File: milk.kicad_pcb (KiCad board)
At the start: 2 copper layers, 19.2 x 39.4 mm, 18 parts, among them J1 USB_C_Receptacle_USB2.0, J2 RGB, J3 DIP-8_W7.62mm_Socket, SW1 SW_Push, SW2 SW_Push, SW3 SW_Push_Reset, U1 ATtiny85-20SU

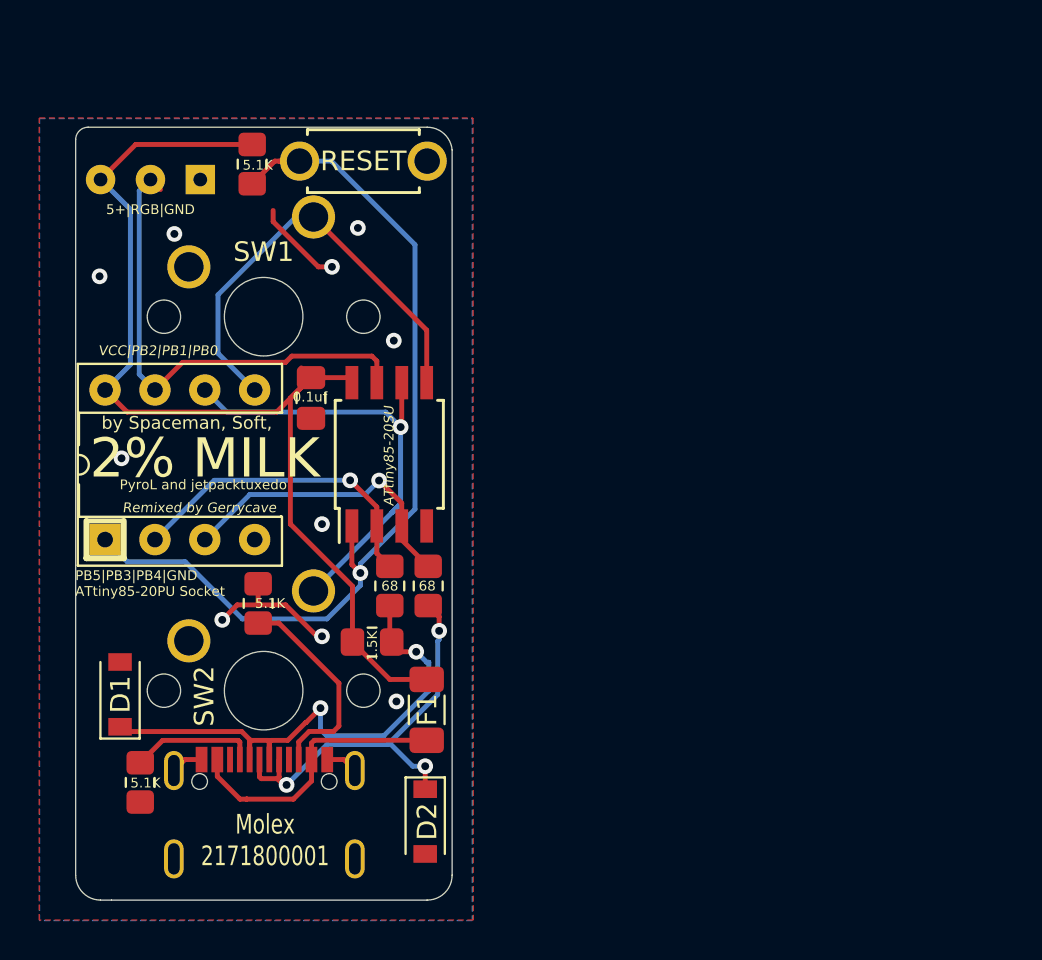
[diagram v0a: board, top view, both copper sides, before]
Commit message: Redo routing, add unsolderable RGB leds
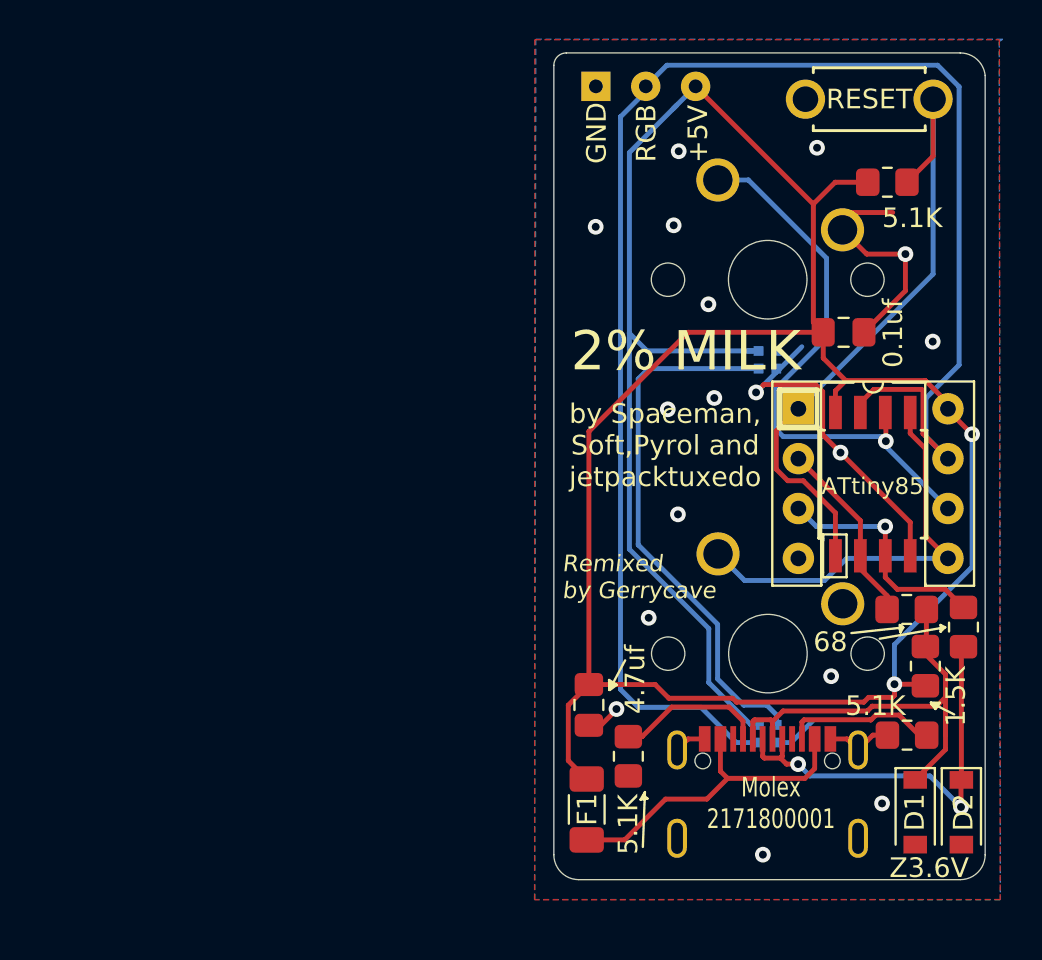
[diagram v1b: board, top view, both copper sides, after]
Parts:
- removed ?: LOGO, silks:40logo
- added C2: 4.7uf, Capacitor_SMD:C_0805_2012Metric_Pad1.18x1.45mm_HandSolder, F.Cu at (197.6, 90.3)
- added D3: SK6805, LED_SMD:LED_SK6812_EC15_1.5x1.5mm, B.Cu at (206.7, 91.7)
- added D4: SK6805, LED_SMD:LED_SK6812_EC15_1.5x1.5mm, B.Cu at (206.7, 72.7)
- added G***: LOGO, footprints:40logo, B.Cu at (201.1, 77.1)
- J3: value DIP-8_W7.62mm_Socket -> DIP-8 Socket
- SW1, SW2: footprint Button_Switch_Keyboard:SW_Cherry_MX_1.00u_PCB -> footprints:SW_Cherry_MX_1.00u_PCB-2mm; moved to B.Cu
- moved D1 40.9 mm to (214.2, 95.7), turned to 270 degrees
- moved J3 35.9 mm to (208.3, 75.2), turned to 0 degrees
- moved R2 33.7 mm to (213.8, 91.8), turned to 0 degrees
- moved R6 32.4 mm to (212.8, 63.6), turned to 180 degrees
- moved SW2 29.4 mm to (204.2, 63.5), turned to 180 degrees
- moved R5 28.2 mm to (214.7, 88.3), turned to 90 degrees
- moved R4 27.3 mm to (216.7, 86.3)
- moved C1 27.3 mm to (210.6, 71.3), turned to 0 degrees
- moved D2 27.3 mm to (216.6, 95.7)
- moved SW1 26.8 mm to (204.2, 82.6), turned to 180 degrees
- moved R3 26.4 mm to (213.8, 85.4), turned to 0 degrees
- moved SW3 26.0 mm to (211.9, 59.4), turned to 0 degrees
- moved J1 25.7 mm to (206.7, 100.0)
- moved R1 24.9 mm to (199.6, 92.9)
- moved U1 24.7 mm to (212.1, 79.0)
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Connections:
- J1 pad : GND -> (no net)
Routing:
- net +5V: track 54.9 -> 140.9 mm, vias 0 -> 2
- net RGB: track 26.3 -> 84.1 mm
- net Net-(D3-Pad1): track 0.00 -> 27.6 mm
- net GND: track 15.2 -> 38.0 mm, vias 10 -> 17
- net RST: track 48.0 -> 33.1 mm, vias 1 -> 0
- net PB3: track 16.4 -> 9.55 mm, vias 1 -> 0
- net D-: track 28.4 -> 23.3 mm, vias 2 -> 0
- net PB1: track 23.9 -> 29.0 mm
- net PB4: track 15.5 -> 12.1 mm
- net Net-(J1-PadB5): track 10.8 -> 7.80 mm
- net VCC: track 14.4 -> 16.8 mm
- net PB0: track 23.0 -> 21.0 mm
- net Net-(J1-PadA5): track 6.47 -> 7.67 mm
- net D+: track 22.0 -> 21.3 mm, vias 3 -> 2
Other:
- board size 19.2 x 39.4 mm -> 22 x 42.1 mm
- board text added: "+5V"
- board text added: "4.7uf"
- board text added: "ATtiny85"
- board text added: "GND"
- board text added: "RGB"
- board text added: "Z3.6V"
- board text added: "by Spaceman, Soft,Pyrol and jetpacktuxedo"
- board text removed: "5+|RGB|GND"
- board text removed: "ATtiny85-20SU"
- board text removed: "PB5|PB3|PB4|GND ATtiny85-20PU Socket"
- board text removed: "PyroL and jetpacktuxedo"
- board text removed: "VCC|PB2|PB1|PB0"
- board text removed: "by Spaceman, Soft,"

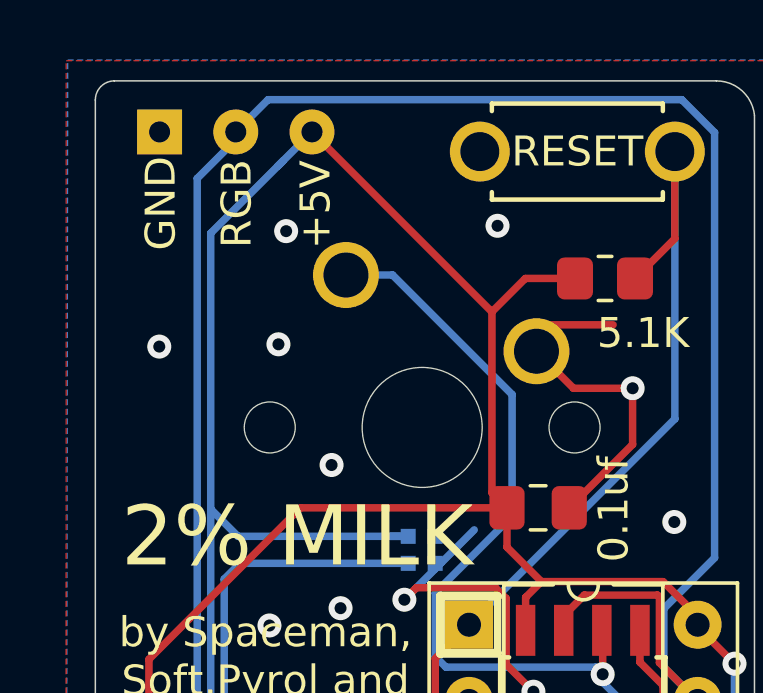
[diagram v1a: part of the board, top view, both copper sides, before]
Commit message: Fix RGB header orientation
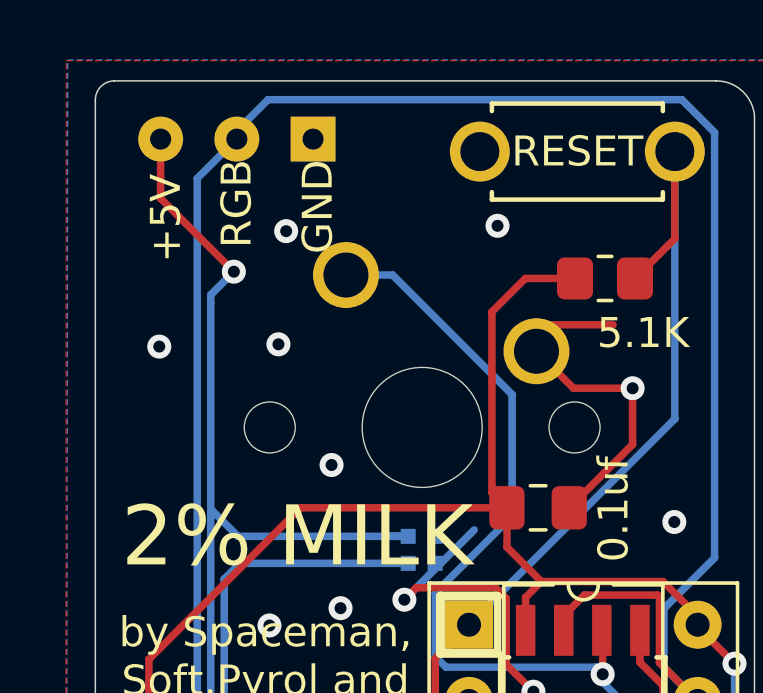
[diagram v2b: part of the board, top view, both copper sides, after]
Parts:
- moved J2 5.12 mm to (203.1, 59.0), turned to 270 degrees
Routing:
- net +5V: track 140.9 -> 131.8 mm, vias 2 -> 3
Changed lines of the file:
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@@
     (thickness 1.6)
     (drawings 64)
-    (tracks 231)
+    (tracks 232)
     (zones 0)
     (modules 21)
@@
       (effects (font (size 1 1) (thickness 0.15)))
     )
-    (fp_text user %R (at 0 0 90) (layer F.Fab)
-      (effects (font (size 0.5 0.5) (thickness 0.08)))
-    )
     (fp_line (start -1 0.625) (end -1 -0.625) (layer F.Fab) (width 0.1))
     (fp_line (start -1 -0.625) (end 1 -0.625) (layer F.Fab) (width 0.1))
@@
     (fp_line (start 1.88 -0.98) (end 1.88 0.98) (layer F.CrtYd) (width 0.05))
     (fp_line (start 1.88 0.98) (end -1.88 0.98) (layer F.CrtYd) (width 0.05))
+    (fp_text user %R (at 0 0 90) (layer F.Fab)
+      (effects (font (size 0.5 0.5) (thickness 0.08)))
+    )
     (pad 2 smd roundrect (at 1.0375 0 90) (size 1.175 1.45) (layers F.Cu F.Paste F.Mask) (roundrect_rratio 0.2127659574468085)
       (net 3 +5V))
@@
     (pad 1 thru_hole rect (at 0 0) (size 1.6 1.6) (drill 0.8) (layers *.Cu *.Mask)
       (net 8 RST))
-    (model ${KISYS3DMOD}/Package_DIP.3dshapes/DIP-8_W7.62mm_Socket.wrl
-      (at (xyz 0 0 0))
-      (scale (xyz 1 1 1))
-      (rotate (xyz 0 0 0))
-    )
   )
   (module footprints:SW_Cherry_MX_1.00u_PCB-2mm (layer B.Cu)
@@
   )
   (module Connector_PinHeader_2.54mm:PinHeader_1x03_P2.54mm_Vertical (layer F.Cu)
-    (at 197.94982 58.7502 90)
+    (at 203.06538 58.98896 270)
     (descr "Through hole straight pin header, 1x03, 2.54mm pitch, single row")
     (tags "Through hole pin header THT 1x03 2.54mm single row")
@@
       (effects (font (size 1 1) (thickness 0.15)))
     )
-    (pad 1 thru_hole rect (at 0 0 90) (size 1.5 1.5) (drill 0.7) (layers *.Cu *.Mask)
-      (net 1 GND))
-    (pad 2 thru_hole circle (at 0 2.54 90) (size 1.5 1.5) (drill 0.7) (layers *.Cu *.Mask)
+    (pad 1 thru_hole rect (at 0 0 270) (size 1.5 1.5) (drill 0.7) (layers *.Cu *.Mask)
+      (net 1 GND))
+    (pad 2 thru_hole circle (at 0 2.54 270) (size 1.5 1.5) (drill 0.7) (layers *.Cu *.Mask)
       (net 9 RGB))
-    (pad 3 thru_hole circle (at 0 5.08 90) (size 1.5 1.5) (drill 0.7) (layers *.Cu *.Mask)
+    (pad 3 thru_hole circle (at 0 5.08 270) (size 1.5 1.5) (drill 0.7) (layers *.Cu *.Mask)
       (net 3 +5V))
   )
@@
     (effects (font (size 1 1) (thickness 0.15)))
   )
-  (gr_text +5V (at 203.1492 61.17082 90) (layer F.SilkS)
+  (gr_text +5V (at 198.16318 61.62548 90) (layer F.SilkS)
     (effects (font (size 1 1) (thickness 0.15)))
   )
@@
     (arrow2b (pts (xy 219.9305 57.05602) (xy 220.516921 58.182524)))
   )
-  (gr_text GND (at 197.98792 61.13018 90) (layer F.SilkS)
+  (gr_text GND (at 203.2254 61.24448 90) (layer F.SilkS)
     (effects (font (size 1 1) (thickness 0.15)))
   )
-  (via (at 216.5477 95.46082) (size 0.8) (drill 0.4) (layers F.Cu B.Cu) (net 5))
-  (via (at 217.11412 76.47432) (size 0.8) (drill 0.4) (layers F.Cu B.Cu) (net 3))
+  (via (at 200.42632 63.40856) (size 0.8) (drill 0.4) (layers F.Cu B.Cu) (net 3))
   (via (at 198.99884 90.46972) (size 0.8) (drill 0.4) (layers F.Cu B.Cu) (net 1))
   (segment (start 202.64504 91.99408) (end 202.08504 92.55408) (width 0.25) (layer F.Cu) (net 1))
@@
   (segment (start 199.41928 97.13588) (end 201.4982 95.05696) (width 0.25) (layer F.Cu) (net 2))
   (segment (start 197.48246 97.13588) (end 199.41928 97.13588) (width 0.25) (layer F.Cu) (net 2))
+  (via (at 217.11412 76.47432) (size 0.8) (drill 0.4) (layers F.Cu B.Cu) (net 3))
   (segment (start 215.88476 74.890688) (end 215.88476 75.17638) (width 0.25) (layer F.Cu) (net 3))
   (segment (start 214.733382 73.73931) (end 215.88476 74.890688) (width 0.25) (layer F.Cu) (net 3))
@@
   (segment (start 203.70038 89.12352) (end 203.70038 86.3727) (width 0.25) (layer B.Cu) (net 3))
   (segment (start 203.70038 86.3727) (end 199.65459 82.32691) (width 0.25) (layer B.Cu) (net 3))
-  (segment (start 199.65459 62.12543) (end 202.06462 59.7154) (width 0.25) (layer B.Cu) (net 3))
-  (segment (start 202.06462 59.7154) (end 203.02982 58.7502) (width 0.25) (layer B.Cu) (net 3))
-  (segment (start 201.88428 59.89574) (end 202.06462 59.7154) (width 0.25) (layer B.Cu) (net 3))
   (segment (start 200.5618 72.22998) (end 199.65459 71.32277) (width 0.25) (layer B.Cu) (net 3))
-  (segment (start 199.65459 71.32277) (end 199.65459 62.12543) (width 0.25) (layer B.Cu) (net 3))
   (segment (start 206.23784 72.22998) (end 200.5618 72.22998) (width 0.25) (layer B.Cu) (net 3))
   (segment (start 199.65459 82.32691) (end 199.65459 71.32277) (width 0.25) (layer B.Cu) (net 3))
@@
   (segment (start 209.027661 70.777821) (end 209.52986 71.28002) (width 0.25) (layer F.Cu) (net 3))
   (segment (start 209.027661 64.748041) (end 209.027661 70.777821) (width 0.25) (layer F.Cu) (net 3))
-  (segment (start 203.02982 58.7502) (end 209.027661 64.748041) (width 0.25) (layer F.Cu) (net 3))
   (segment (start 209.52986 71.28002) (end 202.64628 71.28002) (width 0.25) (layer F.Cu) (net 3))
   (segment (start 197.59422 76.33208) (end 197.59422 89.22258) (width 0.25) (layer F.Cu) (net 3))
@@
   (segment (start 200.968779 89.22258) (end 201.66584 89.919641) (width 0.25) (layer F.Cu) (net 3))
   (segment (start 197.59422 89.22258) (end 200.968779 89.22258) (width 0.25) (layer F.Cu) (net 3))
+  (segment (start 199.65459 64.18029) (end 199.65459 64.45293) (width 0.25) (layer B.Cu) (net 3))
+  (segment (start 200.42632 63.40856) (end 199.65459 64.18029) (width 0.25) (layer B.Cu) (net 3))
+  (segment (start 199.65459 71.32277) (end 199.65459 64.45293) (width 0.25) (layer B.Cu) (net 3))
+  (segment (start 197.98538 60.96762) (end 200.42632 63.40856) (width 0.25) (layer F.Cu) (net 3))
+  (segment (start 197.98538 58.98896) (end 197.98538 60.96762) (width 0.25) (layer F.Cu) (net 3))
   (segment (start 214.78494 87.23452) (end 214.73414 87.28532) (width 0.25) (layer F.Cu) (net 4))
   (segment (start 214.78494 85.39734) (end 214.78494 87.23452) (width 0.25) (layer F.Cu) (net 4))
@@
   (segment (start 215.75915 89.18587) (end 215.75915 90.58287) (width 0.25) (layer F.Cu) (net 4))
   (segment (start 215.75915 88.69714) (end 215.75915 89.18587) (width 0.25) (layer F.Cu) (net 4))
+  (via (at 216.5477 95.46082) (size 0.8) (drill 0.4) (layers F.Cu B.Cu) (net 5))
   (segment (start 216.56802 87.40242) (end 216.6747 87.29574) (width 0.25) (layer F.Cu) (net 5))
   (segment (start 216.56802 94.07906) (end 216.56802 87.40242) (width 0.25) (layer F.Cu) (net 5))

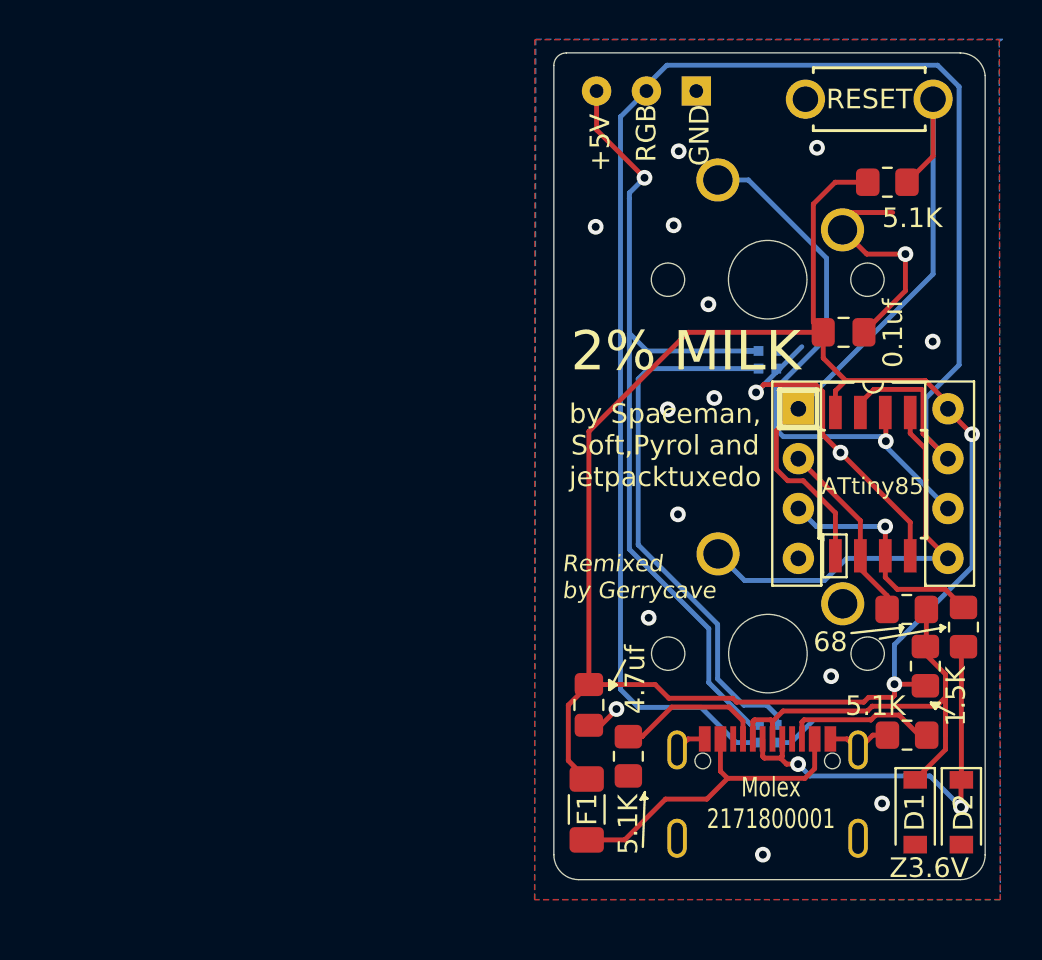
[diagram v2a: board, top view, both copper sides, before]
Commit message: corrections to +5V line, fine-tunning tracing
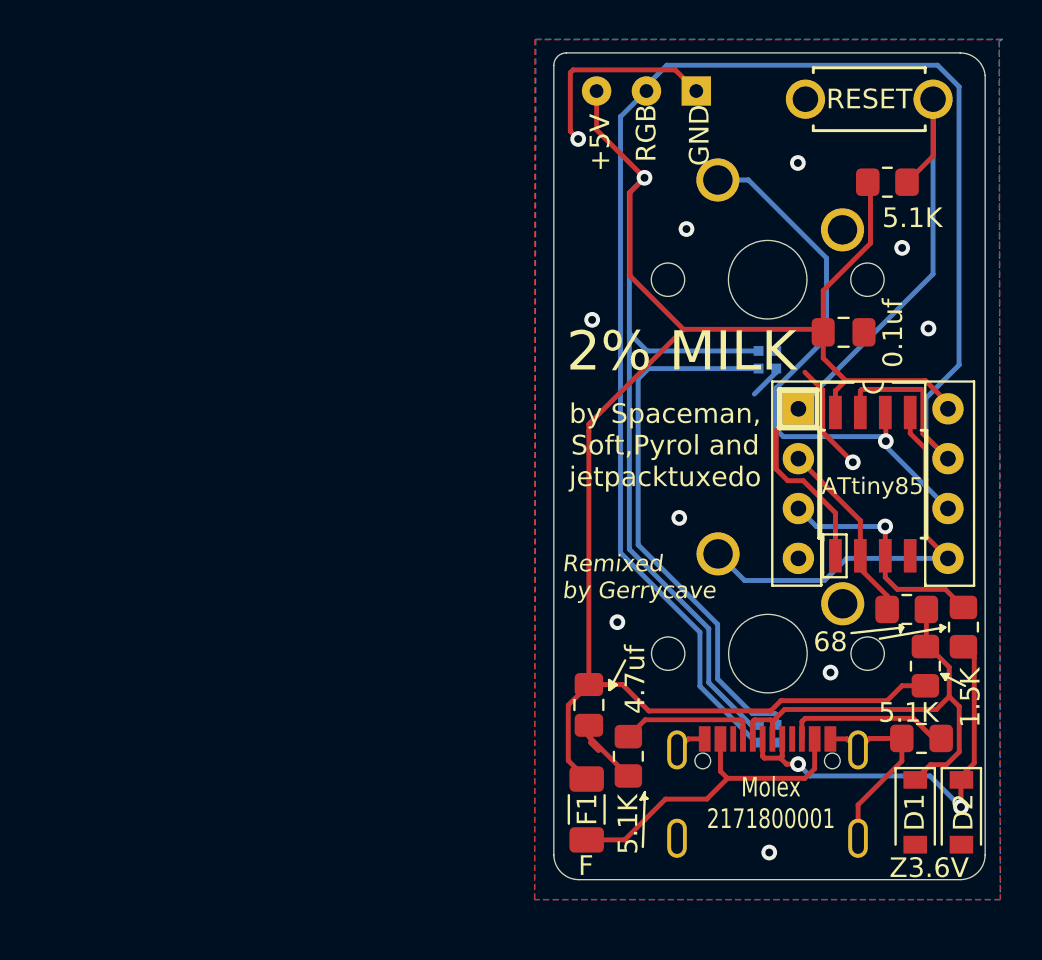
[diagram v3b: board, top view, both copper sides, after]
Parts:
- moved G*** 2.23 mm to (199.2, 78.2)
- moved R2 0.75 mm to (214.5, 92.0)
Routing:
- net +5V: track 131.8 -> 123.5 mm, vias 3 -> 1
- net GND: track 38.0 -> 35.5 mm, vias 17 -> 11
- net RGB: track 84.1 -> 82.4 mm
- net D-: track 23.3 -> 24.6 mm
- net Net-(J1-PadB5): track 7.80 -> 8.47 mm
- net D+: track 21.3 -> 21.9 mm
- net Net-(J1-PadA5): track 7.67 -> 7.12 mm
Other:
- board text added: "F"
